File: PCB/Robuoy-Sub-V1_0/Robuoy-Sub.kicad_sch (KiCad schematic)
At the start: 6 parts

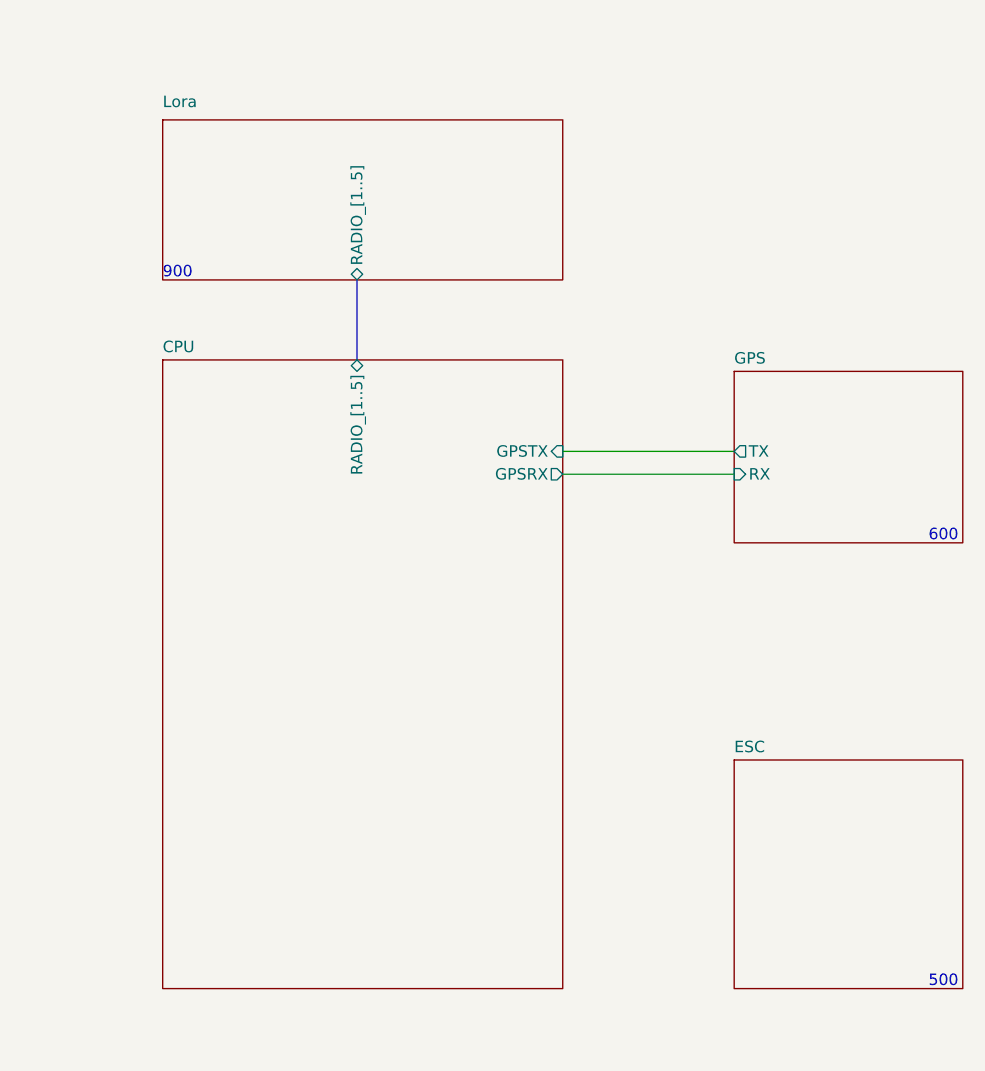
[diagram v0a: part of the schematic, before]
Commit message: Directory renamed. Top finished Sub started
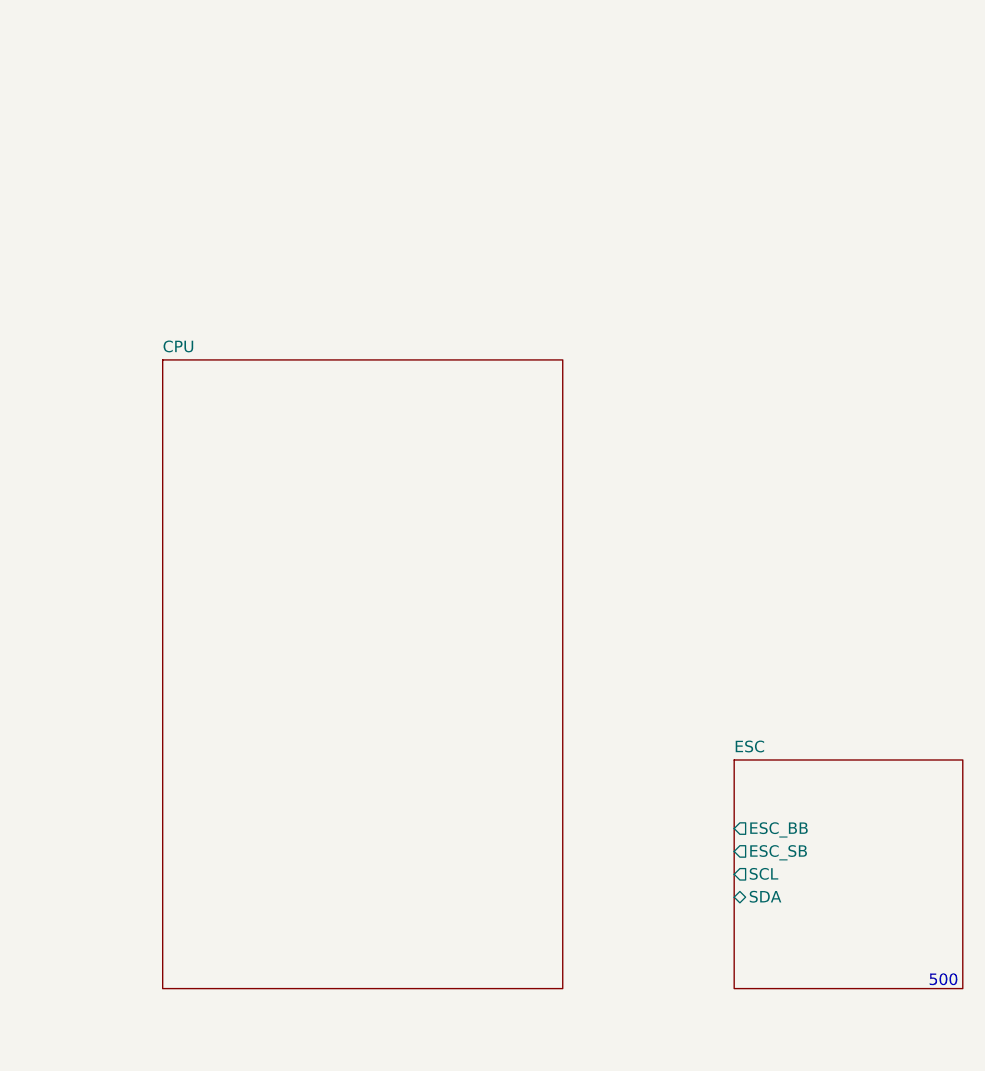
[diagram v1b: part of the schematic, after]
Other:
- removed sheet GPS
- removed sheet Lora
- sheet CPU ports: added none; removed GPSRX, GPSTX, RADIO_[1..5]
- sheet ESC ports: added ESC_BB, ESC_SB, SCL, SDA; removed none
- note removed: "600"
- note removed: "900"
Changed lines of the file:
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@@
 		(at 45.72 191.77)
-	)
-	(wire
-		(pts
-			(xy 139.7 60.96) (xy 158.75 60.96)
-		)
-		(stroke
-			(width 0)
-			(type default)
-		)
-	)
-	(bus
-		(pts
-			(xy 116.84 41.91) (xy 116.84 50.8)
-		)
-		(stroke
-			(width 0)
-			(type default)
-		)
-	)
-	(wire
-		(pts
-			(xy 139.7 63.5) (xy 158.75 63.5)
-		)
-		(stroke
-			(width 0)
-			(type default)
-		)
 	)
 	(text "300"
@@
 		)
 	)
-	(text "600"
-		(exclude_from_sim no)
-		(at 180.34 71.12 0)
-		(effects
-			(font
-				(size 1.27 1.27)
-			)
-			(justify left bottom)
-		)
-	)
 	(text "ESP32\nLORA\nGPS\nCOMPASS\nGIRO\nACCELOROMETER\nBATTERY MONITOR\nPOWERSUPPY 12V 5V 3.3V\nMODE SWITCH\nLEDSTRIP\nLipo monitoring\n"
 		(exclude_from_sim no)
 		(at 17.145 35.56 0)
-		(effects
-			(font
-				(size 1.27 1.27)
-			)
-			(justify left bottom)
-		)
-	)
-	(text "900"
-		(exclude_from_sim no)
-		(at 95.25 41.91 0)
 		(effects
 			(font
@@
 		)
 		(instances
-			(project "Robuoy"
+			(project "Robuoy-Sub"
 				(path "/77bea089-a6ae-4a6f-b95b-7a9010ad7c5d"
 					(reference "TP2")
@@
 		)
 		(instances
-			(project "Robuoy"
+			(project "Robuoy-Sub"
 				(path "/77bea089-a6ae-4a6f-b95b-7a9010ad7c5d"
 					(reference "H1004")
@@
 		)
 		(instances
-			(project "Robuoy"
+			(project "Robuoy-Sub"
 				(path "/77bea089-a6ae-4a6f-b95b-7a9010ad7c5d"
 					(reference "H1003")
@@
 		)
 		(instances
-			(project "Robuoy"
+			(project "Robuoy-Sub"
 				(path "/77bea089-a6ae-4a6f-b95b-7a9010ad7c5d"
 					(reference "TP1")
@@
 		)
 		(instances
-			(project "Robuoy"
+			(project "Robuoy-Sub"
 				(path "/77bea089-a6ae-4a6f-b95b-7a9010ad7c5d"
 					(reference "H1002")
@@
 		)
 		(instances
-			(project "Robuoy"
+			(project "Robuoy-Sub"
 				(path "/77bea089-a6ae-4a6f-b95b-7a9010ad7c5d"
 					(reference "H1001")
 					(unit 1)
-				)
-			)
-		)
-	)
-	(sheet
-		(at 95.25 24.13)
-		(size 44.45 17.78)
-		(stroke
-			(width 0.1524)
-			(type solid)
-		)
-		(fill
-			(color 0 0 0 0.0000)
-		)
-		(property "Sheetname" "Lora"
-			(at 95.25 22.86 0)
-			(effects
-				(font
-					(size 1.27 1.27)
-				)
-				(justify left bottom)
-			)
-		)
-		(property "Sheetfile" "Lora.kicad_sch"
-			(at 140.2846 41.91 90)
-			(effects
-				(font
-					(size 1.27 1.27)
-				)
-				(justify left top)
-				(hide yes)
-			)
-		)
-		(pin "RADIO_[1..5]" bidirectional
-			(at 116.84 41.91 270)
-			(effects
-				(font
-					(size 1.27 1.27)
-				)
-				(justify left)
-			)
-		)
-		(instances
-			(project "Robuoy"
-				(path "/77bea089-a6ae-4a6f-b95b-7a9010ad7c5d"
-					(page "6")
 				)
 			)
@@
 			)
 		)
-		(pin "GPSRX" output
-			(at 139.7 63.5 0)
-			(effects
-				(font
-					(size 1.27 1.27)
-				)
-				(justify right)
-			)
-		)
-		(pin "GPSTX" input
-			(at 139.7 60.96 0)
-			(effects
-				(font
-					(size 1.27 1.27)
-				)
-				(justify right)
-			)
-		)
-		(pin "RADIO_[1..5]" bidirectional
-			(at 116.84 50.8 90)
-			(effects
-				(font
-					(size 1.27 1.27)
-				)
-				(justify right)
-			)
-		)
-		(instances
-			(project "Robuoy"
+		(instances
+			(project "Robuoy-Sub"
 				(path "/77bea089-a6ae-4a6f-b95b-7a9010ad7c5d"
 					(page "1")
-				)
-			)
-		)
-	)
-	(sheet
-		(at 158.75 52.07)
-		(size 25.4 19.05)
-		(fields_autoplaced yes)
-		(stroke
-			(width 0.1524)
-			(type solid)
-		)
-		(fill
-			(color 0 0 0 0.0000)
-		)
-		(property "Sheetname" "GPS"
-			(at 158.75 51.3584 0)
-			(effects
-				(font
-					(size 1.27 1.27)
-				)
-				(justify left bottom)
-			)
-		)
-		(property "Sheetfile" "Gps_sch.kicad_sch"
-			(at 158.75 71.7046 0)
-			(effects
-				(font
-					(size 1.27 1.27)
-				)
-				(justify left top)
-				(hide yes)
-			)
-		)
-		(pin "RX" input
-			(at 158.75 63.5 180)
-			(effects
-				(font
-					(size 1.27 1.27)
-				)
-				(justify left)
-			)
-		)
-		(pin "TX" output
-			(at 158.75 60.96 180)
-			(effects
-				(font
-					(size 1.27 1.27)
-				)
-				(justify left)
-			)
-		)
-		(instances
-			(project "Robuoy"
-				(path "/77bea089-a6ae-4a6f-b95b-7a9010ad7c5d"
-					(page "5")
 				)
 			)
@@
 		)
 		(instances
-			(project "Robuoy"
+			(project "Robuoy-Sub"
 				(path "/77bea089-a6ae-4a6f-b95b-7a9010ad7c5d"
 					(page "2")
@@
 			)
 		)
-		(instances
-			(project "Robuoy"
+		(pin "ESC_BB" output
+			(at 158.75 102.87 180)
+			(effects
+				(font
+					(size 1.27 1.27)
+				)
+				(justify left)
+			)
+		)
+		(pin "ESC_SB" output
+			(at 158.75 105.41 180)
+			(effects
+				(font
+					(size 1.27 1.27)
+				)
+				(justify left)
+			)
+		)
+		(pin "SCL" output
+			(at 158.75 107.95 180)
+			(effects
+				(font
+					(size 1.27 1.27)
+				)
+				(justify left)
+			)
+		)
+		(pin "SDA" bidirectional
+			(at 158.75 110.49 180)
+			(effects
+				(font
+					(size 1.27 1.27)
+				)
+				(justify left)
+			)
+		)
+		(instances
+			(project "Robuoy-Sub"
 				(path "/77bea089-a6ae-4a6f-b95b-7a9010ad7c5d"
 					(page "4")

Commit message: Schematic changes not yet finished!
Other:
- removed sheet ESC
- sheet CPU ports: added PWR_ESC_BB, PWR_ESC_SB, Vbatt; removed none
- sheet PSU ports: added PWR_ESC_BB, PWR_ESC_SB, Vbatt; removed none
- note removed: "500"
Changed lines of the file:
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@@
 		(at 45.72 191.77)
+	)
+	(wire
+		(pts
+			(xy 115.57 120.65) (xy 115.57 161.29)
+		)
+		(stroke
+			(width 0)
+			(type default)
+		)
+	)
+	(wire
+		(pts
+			(xy 113.03 120.65) (xy 113.03 161.29)
+		)
+		(stroke
+			(width 0)
+			(type default)
+		)
+	)
+	(wire
+		(pts
+			(xy 118.11 120.65) (xy 118.11 161.29)
+		)
+		(stroke
+			(width 0)
+			(type default)
+		)
 	)
 	(text "300"
@@
 		(exclude_from_sim no)
 		(at 17.145 35.56 0)
-		(effects
-			(font
-				(size 1.27 1.27)
-			)
-			(justify left bottom)
-		)
-	)
-	(text "500"
-		(exclude_from_sim no)
-		(at 180.34 120.65 0)
 		(effects
 			(font
@@
 			)
 		)
+		(pin "PWR_ESC_BB" input
+			(at 113.03 120.65 270)
+			(effects
+				(font
+					(size 1.27 1.27)
+				)
+				(justify left)
+			)
+		)
+		(pin "PWR_ESC_SB" input
+			(at 115.57 120.65 270)
+			(effects
+				(font
+					(size 1.27 1.27)
+				)
+				(justify left)
+			)
+		)
+		(pin "Vbatt" output
+			(at 118.11 120.65 270)
+			(effects
+				(font
+					(size 1.27 1.27)
+				)
+				(justify left)
+			)
+		)
 		(instances
 			(project "Robuoy-Sub"
@@
 			)
 		)
+		(pin "PWR_ESC_SB" output
+			(at 115.57 161.29 90)
+			(effects
+				(font
+					(size 1.27 1.27)
+				)
+				(justify right)
+			)
+		)
+		(pin "PWR_ESC_BB" output
+			(at 113.03 161.29 90)
+			(effects
+				(font
+					(size 1.27 1.27)
+				)
+				(justify right)
+			)
+		)
+		(pin "Vbatt" input
+			(at 118.11 161.29 90)
+			(effects
+				(font
+					(size 1.27 1.27)
+				)
+				(justify right)
+			)
+		)
 		(instances
 			(project "Robuoy-Sub"
@@
 				)
 			)
-		)
-	)
-	(sheet
-		(at 158.75 95.25)
-		(size 25.4 25.4)
-		(fields_autoplaced yes)
-		(stroke
-			(width 0.1524)
-			(type solid)
-		)
-		(fill
-			(color 0 0 0 0.0000)
-		)
-		(property "Sheetname" "ESC"
-			(at 158.75 94.5384 0)
-			(effects
-				(font
-					(size 1.27 1.27)
-				)
-				(justify left bottom)
-			)
-		)
-		(property "Sheetfile" "Esc_sch.kicad_sch"
-			(at 158.75 121.2346 0)
-			(effects
-				(font
-					(size 1.27 1.27)
-				)
-				(justify left top)
-				(hide yes)
-			)
-		)
-		(pin "ESC_BB" output
-			(at 158.75 102.87 180)
-			(effects
-				(font
-					(size 1.27 1.27)
-				)
-				(justify left)
-			)
-		)
-		(pin "ESC_SB" output
-			(at 158.75 105.41 180)
-			(effects
-				(font
-					(size 1.27 1.27)
-				)
-				(justify left)
-			)
-		)
-		(pin "SCL" output
-			(at 158.75 107.95 180)
-			(effects
-				(font
-					(size 1.27 1.27)
-				)
-				(justify left)
-			)
-		)
-		(pin "SDA" bidirectional
-			(at 158.75 110.49 180)
-			(effects
-				(font
-					(size 1.27 1.27)
-				)
-				(justify left)
-			)
-		)
-		(instances
-			(project "Robuoy-Sub"
-				(path "/77bea089-a6ae-4a6f-b95b-7a9010ad7c5d"
-					(page "4")
-				)
-			)

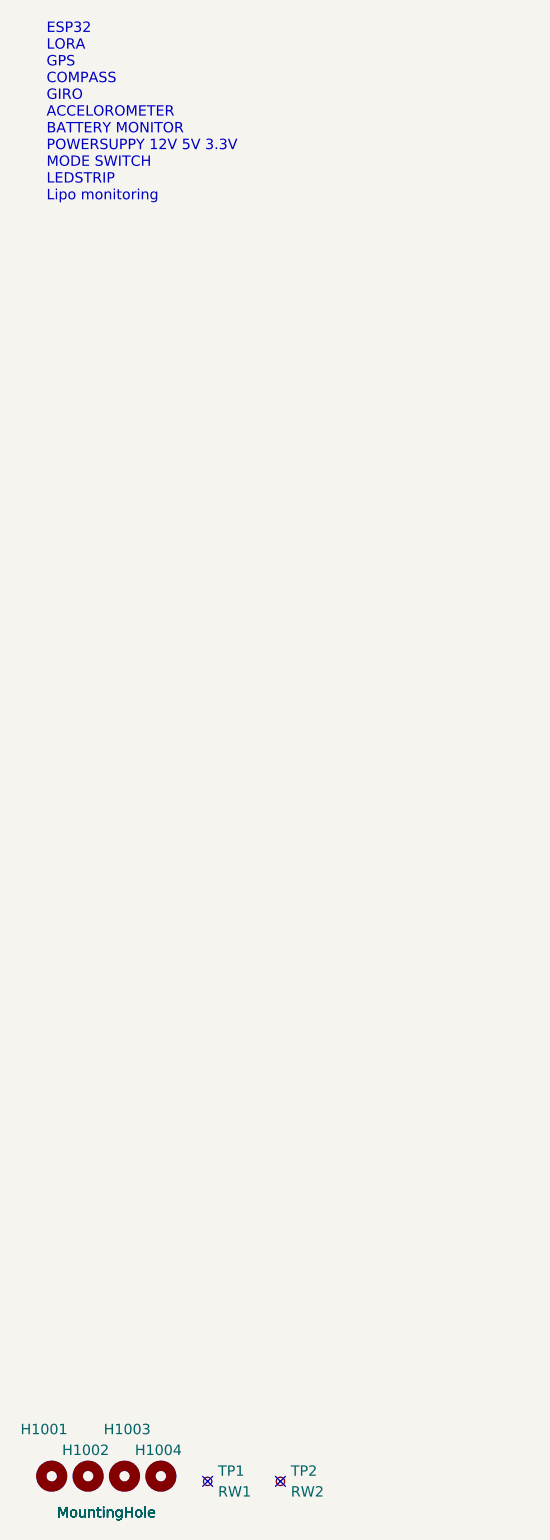
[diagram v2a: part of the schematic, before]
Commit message: Sub ready for routing
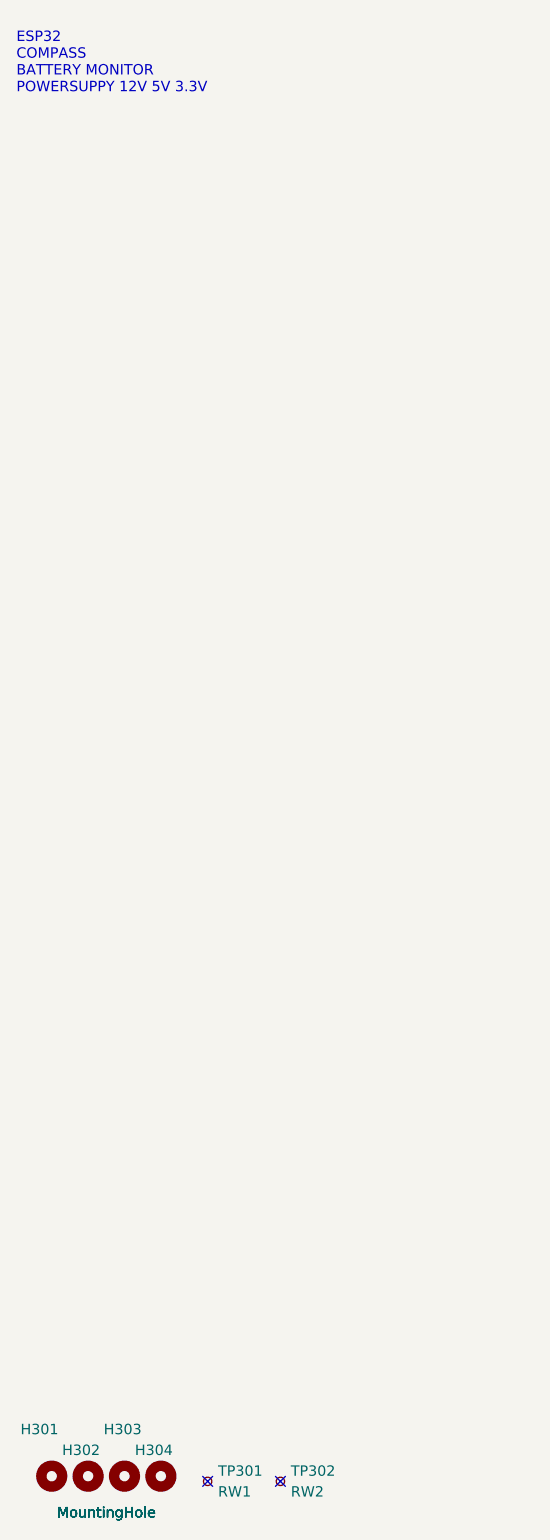
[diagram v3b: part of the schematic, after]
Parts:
- renumbered H1001 to H301, H1002 to H302, H1003 to H303, H1004 to H304, TP1 to TP301, TP2 to TP302
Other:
- note added: "ESP32 COMPASS BATTERY MONITOR POWERSUPPY 12V 5V 3.3V"
- note removed: "ESP32 LORA GPS COMPASS GIRO ACCELOROMETER BATTERY MONITOR POWERSUPPY 12V 5V 3.3V MODE SWITCH LEDSTRIP Lipo monitoring"
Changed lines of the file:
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@@
 		)
 	)
-	(text "ESP32\nLORA\nGPS\nCOMPASS\nGIRO\nACCELOROMETER\nBATTERY MONITOR\nPOWERSUPPY 12V 5V 3.3V\nMODE SWITCH\nLEDSTRIP\nLipo monitoring\n"
-		(exclude_from_sim no)
-		(at 17.145 35.56 0)
+	(text "ESP32\nCOMPASS\nBATTERY MONITOR\nPOWERSUPPY 12V 5V 3.3V\n"
+		(exclude_from_sim no)
+		(at 13.462 22.352 0)
 		(effects
 			(font
@@
 		(dnp no)
 		(fields_autoplaced yes)
-		(property "Reference" "TP2"
+		(property "Reference" "TP302"
 			(at 46.99 190.5 0)
 			(effects
@@
 			(project "Robuoy-Sub"
 				(path "/77bea089-a6ae-4a6f-b95b-7a9010ad7c5d"
-					(reference "TP2")
+					(reference "TP302")
 					(unit 1)
 				)
@@
 		(on_board yes)
 		(dnp no)
-		(property "Reference" "H1004"
+		(property "Reference" "H304"
 			(at 27.94 187.96 0)
 			(effects
@@
 			)
 		)
-		(instances
-			(project "Robuoy-Sub"
-				(path "/77bea089-a6ae-4a6f-b95b-7a9010ad7c5d"
-					(reference "H1004")
+		(property "JLCS" ""
+			(at 31.115 191.135 0)
+			(effects
+				(font
+					(size 1.27 1.27)
+				)
+				(hide yes)
+			)
+		)
+		(instances
+			(project "Robuoy-Sub"
+				(path "/77bea089-a6ae-4a6f-b95b-7a9010ad7c5d"
+					(reference "H304")
 					(unit 1)
 				)
@@
 		(on_board yes)
 		(dnp no)
-		(property "Reference" "H1003"
+		(property "Reference" "H303"
 			(at 24.13 185.42 0)
 			(effects
@@
 			)
 		)
-		(instances
-			(project "Robuoy-Sub"
-				(path "/77bea089-a6ae-4a6f-b95b-7a9010ad7c5d"
-					(reference "H1003")
+		(property "JLCS" ""
+			(at 26.67 191.135 0)
+			(effects
+				(font
+					(size 1.27 1.27)
+				)
+				(hide yes)
+			)
+		)
+		(instances
+			(project "Robuoy-Sub"
+				(path "/77bea089-a6ae-4a6f-b95b-7a9010ad7c5d"
+					(reference "H303")
 					(unit 1)
 				)
@@
 		(dnp no)
 		(fields_autoplaced yes)
-		(property "Reference" "TP1"
+		(property "Reference" "TP301"
 			(at 38.1 190.5 0)
 			(effects
@@
 			(project "Robuoy-Sub"
 				(path "/77bea089-a6ae-4a6f-b95b-7a9010ad7c5d"
-					(reference "TP1")
+					(reference "TP301")
 					(unit 1)
 				)
@@
 		(on_board yes)
 		(dnp no)
-		(property "Reference" "H1002"
+		(property "Reference" "H302"
 			(at 19.05 187.96 0)
 			(effects
@@
 			)
 		)
-		(instances
-			(project "Robuoy-Sub"
-				(path "/77bea089-a6ae-4a6f-b95b-7a9010ad7c5d"
-					(reference "H1002")
+		(property "JLCS" ""
+			(at 22.225 191.135 0)
+			(effects
+				(font
+					(size 1.27 1.27)
+				)
+				(hide yes)
+			)
+		)
+		(instances
+			(project "Robuoy-Sub"
+				(path "/77bea089-a6ae-4a6f-b95b-7a9010ad7c5d"
+					(reference "H302")
 					(unit 1)
 				)
@@
 		(on_board yes)
 		(dnp no)
-		(property "Reference" "H1001"
+		(property "Reference" "H301"
 			(at 13.97 185.42 0)
 			(effects
@@
 			)
 		)
-		(instances
-			(project "Robuoy-Sub"
-				(path "/77bea089-a6ae-4a6f-b95b-7a9010ad7c5d"
-					(reference "H1001")
-					(unit 1)
-				)
+		(property "JLCS" ""
+			(at 17.78 191.135 0)
+			(effects
+				(font
+					(size 1.27 1.27)
+				)
+				(hide yes)
+			)
+		)
+		(instances
+			(project "Robuoy-Sub"
+				(path "/77bea089-a6ae-4a6f-b95b-7a9010ad7c5d"
+					(reference "H301")
+					(unit 1)
+				)

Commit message: Pcb edditing
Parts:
- added H305, H306, H307, H308: MountingHole, A_Mechanical:NPTH_M3, symbol Mechanical:MountingHole
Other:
- moved on the sheet: H301, H302, H303, H304, TP301, TP302

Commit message: Som more routing
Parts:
- removed H305, H306, H307, H308: MountingHole, A_Mechanical:NPTH_M3, symbol Mechanical:MountingHole
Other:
- sheet CPU ports: added Vsamp; removed Vbatt
- sheet PSU ports: added Vsamp; removed Vbatt
